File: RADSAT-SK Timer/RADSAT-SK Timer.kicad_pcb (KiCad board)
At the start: 2 copper layers, 90.2 x 95.9 mm, 97 parts, among them J101 Conn_02x26_Odd_Even, J103 Conn_02x26_Odd_Even, J201 Conn_01x04, J203 Conn_01x02, J204 USB_B_Micro, Q101 IRLML2060, Q102 IRLML2060, Q103 IRLML2060, Q104 IRLML2060, Q105 IRLML2060, Q106 IRLML2060, Q107 IRLML2060, Q108 IRLML2060, Q109 IRLML2060, Q201 IRLML2060, SW201 SW_Push, SW202 SW_Push, SW203 SW_Push, SW204 SW_Push, SW205 SW_Push, SW206 SW_Push, U101 LM397MF, U102 LM397MF, U103 LM397MF, U104 CD4052B, U202 LTC3440EMSPBF

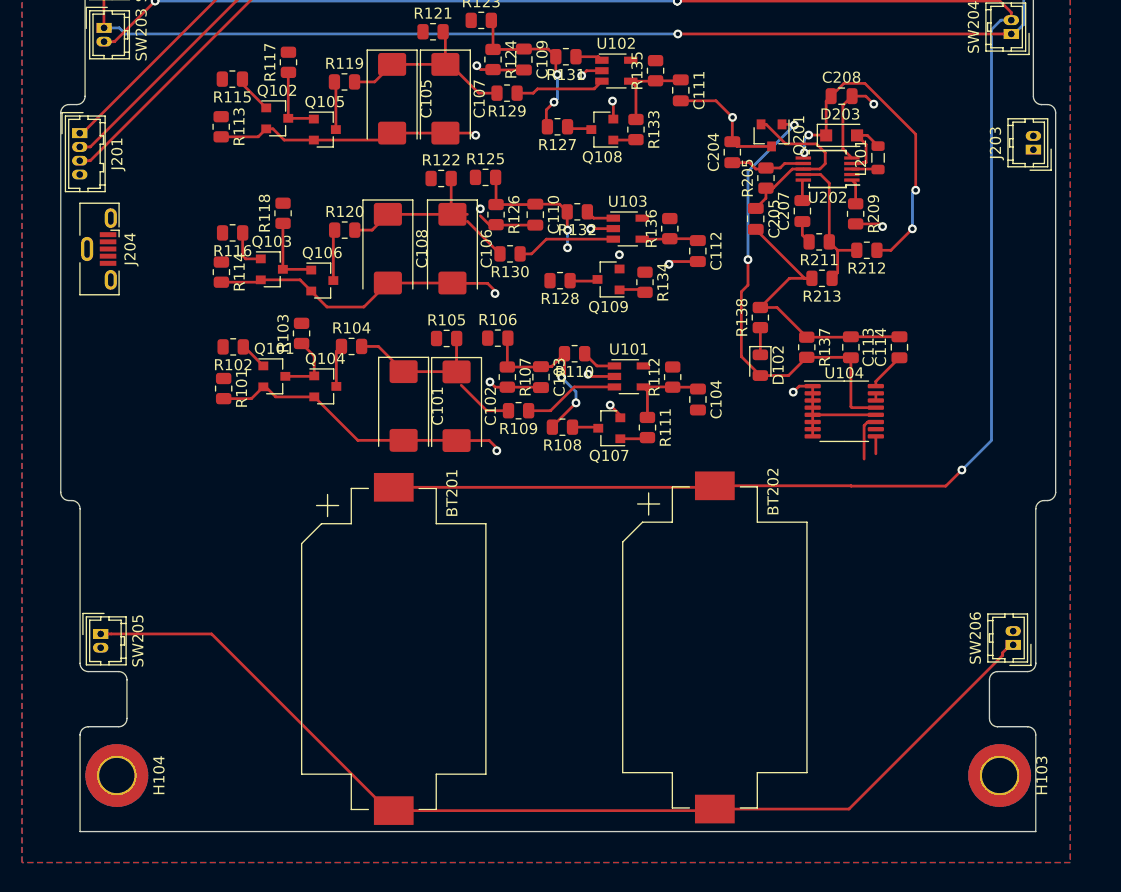
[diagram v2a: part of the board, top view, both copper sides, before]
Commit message: Schematic: Added- 2 more inhibit ports Added- RBF Ports In and Out Connected USb Charger to connector H1-32. Layout: Port positioning and adjustments to some existing circuitry for better tracing.
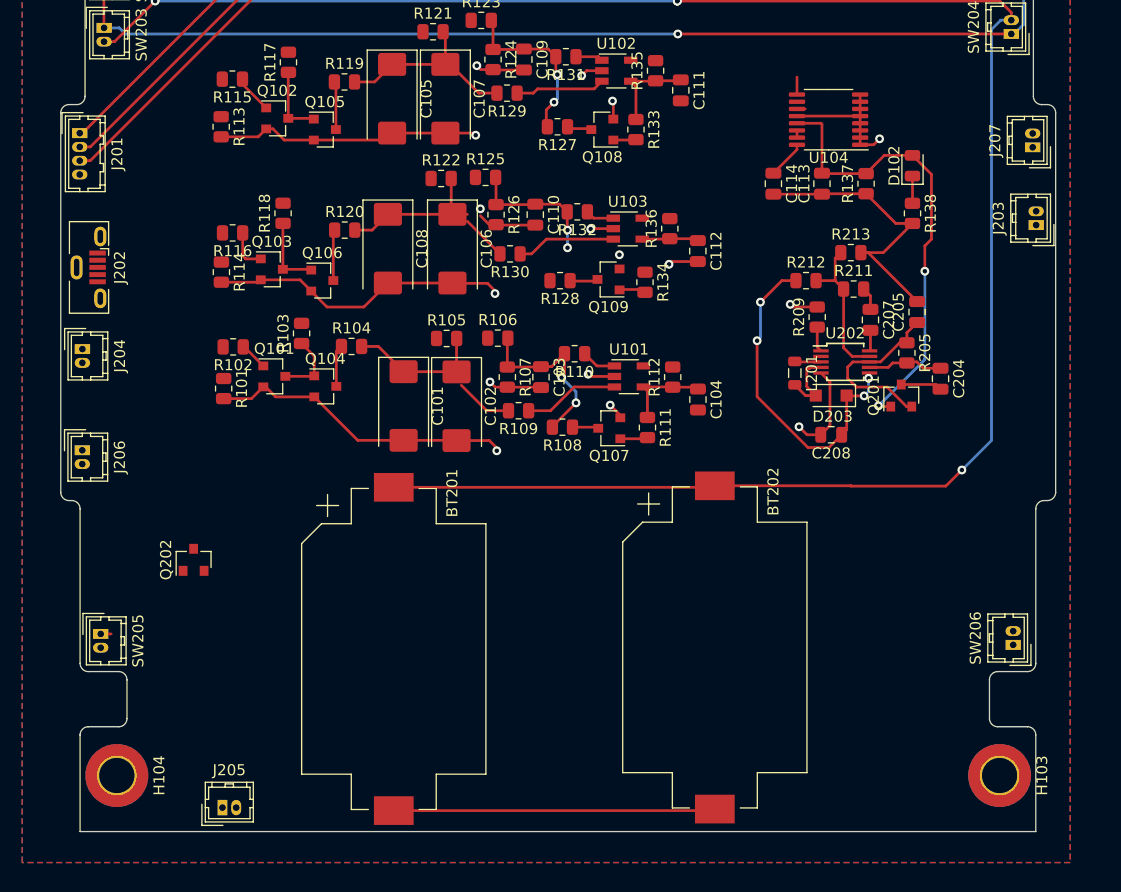
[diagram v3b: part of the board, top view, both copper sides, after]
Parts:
- added J202: USB_B_Micro, Connector_USB:USB_Micro-B_Molex-105133-0001, F.Cu at (37.3, 94.8)
- added J205: Conn_01x02, Connector_Hirose:Hirose_DF13-02P-1.25DSA_1x02_P1.25mm_Vertical, F.Cu at (49.5, 143.7)
- added J206: Conn_01x02, Connector_Hirose:Hirose_DF13-02P-1.25DSA_1x02_P1.25mm_Vertical, F.Cu at (36.8, 111.3)
- added J207: Conn_01x02, Connector_Hirose:Hirose_DF13-02P-1.25DSA_1x02_P1.25mm_Vertical, F.Cu at (122.9, 83.9)
- added Q202: IRLML2060, Package_TO_SOT_SMD:SOT-23, F.Cu at (46.9, 121.3)
- J204: value USB_B_Micro -> Conn_01x02; footprint Connector_USB:USB_Micro-B_Molex-105133-0001 -> Connector_Hirose:Hirose_DF13-02P-1.25DSA_1x02_P1.25mm_Vertical
- moved C208 30.7 mm to (104.7, 109.9), turned to 180 degrees
- moved C204 27.9 mm to (114.6, 104.8), turned to 270 degrees
- moved U104 26.5 mm to (104.4, 81.4), turned to 180 degrees
- moved Q201 26.3 mm to (111.0, 106.4), turned to 90 degrees
- moved D203 23.6 mm to (104.7, 106.4), turned to 180 degrees
- moved D102 22.7 mm to (112.0, 85.5), turned to 90 degrees
- moved L201 20.9 mm to (101.4, 104.3), turned to 270 degrees
- moved R205 20.4 mm to (111.5, 102.5), turned to 270 degrees
- moved C114 18.7 mm to (99.4, 87.2), turned to 270 degrees
- moved U202 17.6 mm to (105.9, 103.3), turned to 0 degrees
- moved C205 16.9 mm to (112.4, 98.8), turned to 90 degrees
- moved R138 16.7 mm to (112.0, 89.9), turned to 270 degrees
- moved R137 15.8 mm to (107.8, 87.2), turned to 90 degrees
- moved C113 15.1 mm to (103.8, 87.2), turned to 270 degrees
- moved C207 11.6 mm to (108.2, 99.5), turned to 270 degrees
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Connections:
- J101 pad 32: (no net) -> USB_Charge
- J204 pad 1: (no net) -> BUS_EN
- J204 pad 2: (no net) -> GND
- SW205 pad 1: Net-(BT201-Pad2) -> Net-(Q202-Pad3)
- SW206 pad 1: Net-(BT201-Pad2) -> Net-(Q202-Pad3)
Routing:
- net Net-(BT201-Pad2): track 95.7 -> 29.7 mm
- net GND: track 172.2 -> 164.7 mm, vias 18 -> 17
- net +BATT: track 38.2 -> 34.7 mm
- net Net-(Q202-Pad3): track 0.00 -> 1.20 mm

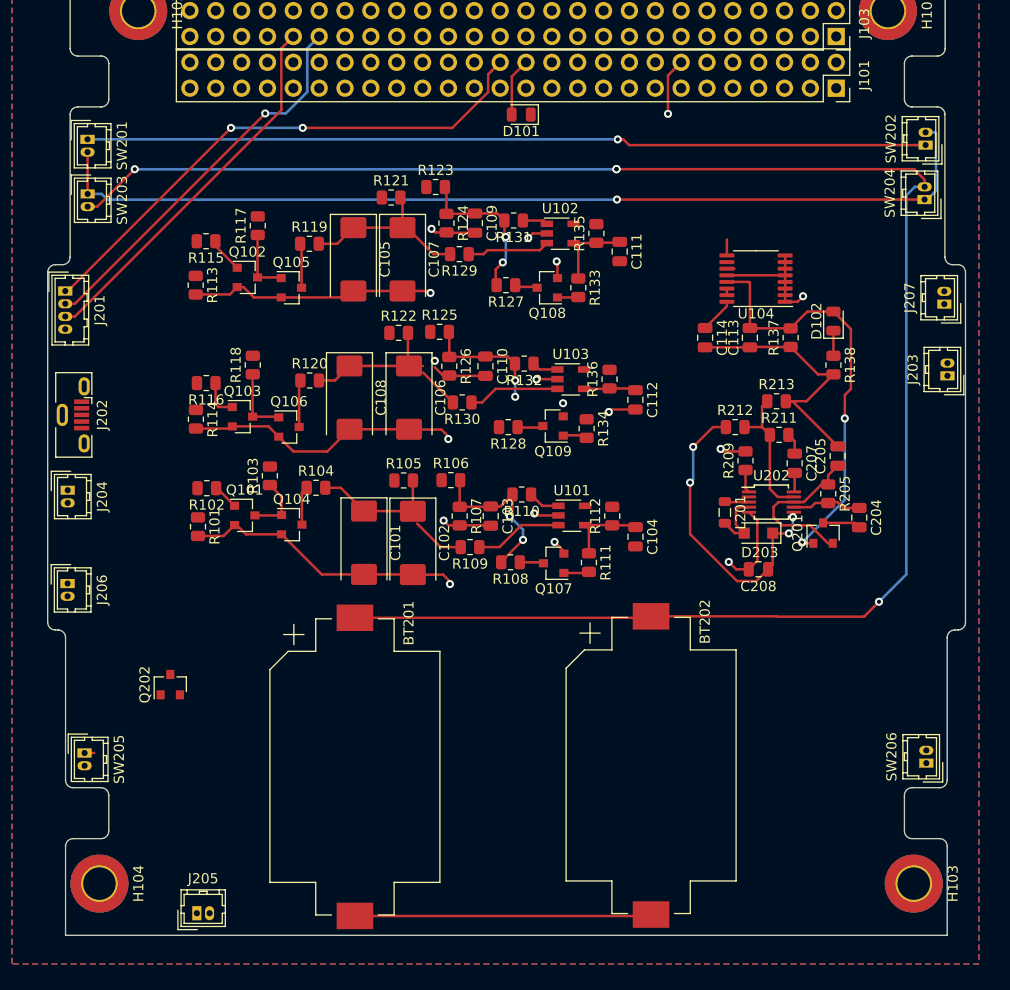
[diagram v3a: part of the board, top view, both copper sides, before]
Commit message: Retraced the board
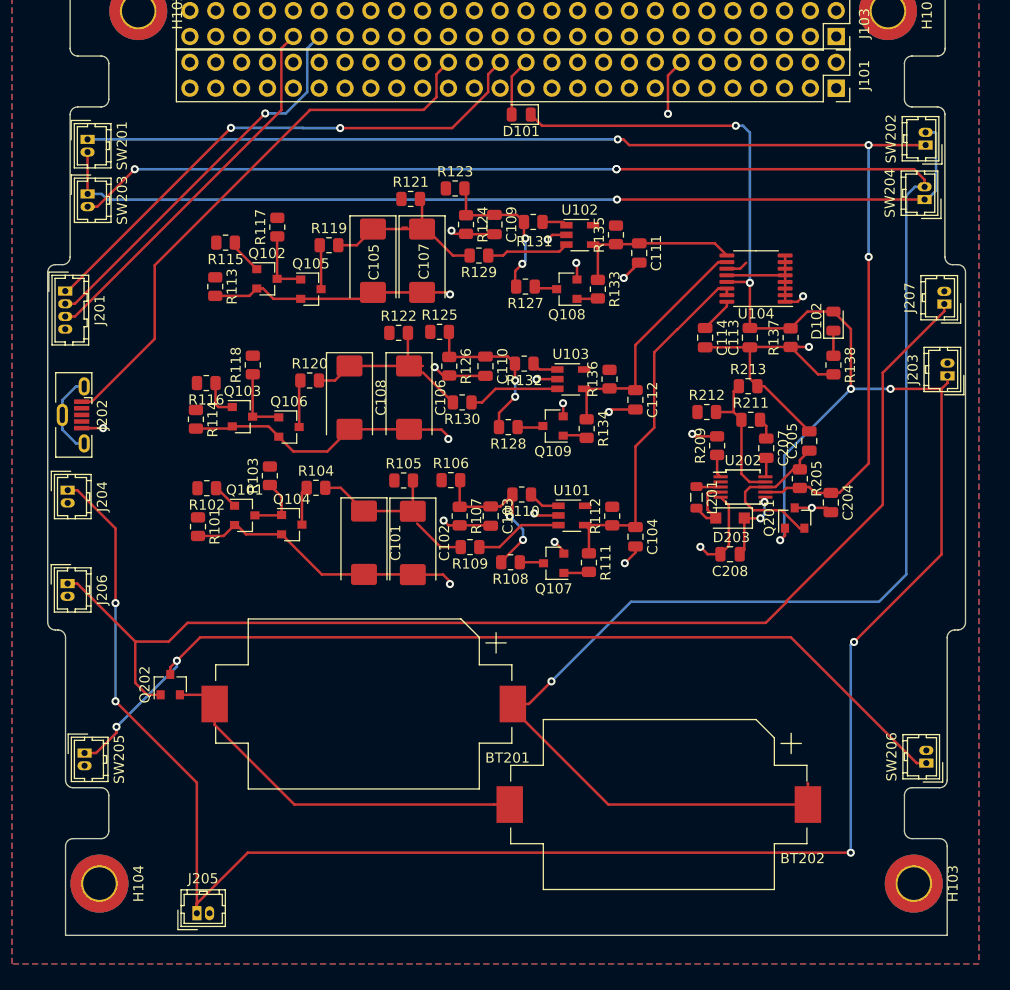
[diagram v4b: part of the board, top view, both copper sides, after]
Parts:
- moved BT201 6.24 mm to (65.9, 123.2), turned to 180 degrees
- moved BT202 3.91 mm to (94.9, 133.0), turned to 180 degrees
- moved C204 3.16 mm to (111.8, 103.4)
- moved C205 3.16 mm to (109.7, 97.3)
- moved Q201 3.16 mm to (108.2, 104.9)
- moved L201 3.16 mm to (98.6, 102.9)
- moved R205 3.16 mm to (108.7, 101.0)
- moved R209 3.16 mm to (100.6, 97.8)
- moved R213 3.16 mm to (103.6, 91.9)
- moved C207 3.16 mm to (105.4, 98.0)
- moved C208 3.16 mm to (101.9, 108.4)
- moved D203 3.16 mm to (101.9, 104.9)
- moved R211 3.16 mm to (103.9, 95.2)
- moved R212 3.16 mm to (99.6, 94.5)
- moved U202 3.16 mm to (103.1, 101.8)
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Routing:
- net BUS_EN: track 42.2 -> 254.5 mm, vias 2 -> 9
- net /RADSAT-SK Timer 2/RBF: track 0.00 -> 117.3 mm
- net Net-(Q202-Pad3): track 1.20 -> 95.2 mm, vias 0 -> 2
- net USB_Charge: track 0.00 -> 55.4 mm
- net Net-(C204-Pad1): track 89.5 -> 125.6 mm, vias 1 -> 3
- net Timer_A_out: track 8.59 -> 36.6 mm
- net Net-(BT201-Pad1): track 180.3 -> 204.1 mm
- net +BATT: track 34.7 -> 14.0 mm, vias 4 -> 2
- net Timer_C_out: track 5.18 -> 25.1 mm
- net Net-(BT201-Pad2): track 29.7 -> 38.1 mm
- net Net-(J202-Pad6): track 0.00 -> 8.32 mm
- net Timer_B_out: track 9.83 -> 17.4 mm
- net GND: track 164.7 -> 171.6 mm, vias 17 -> 22
- net Net-(C110-Pad1): track 12.3 -> 15.9 mm

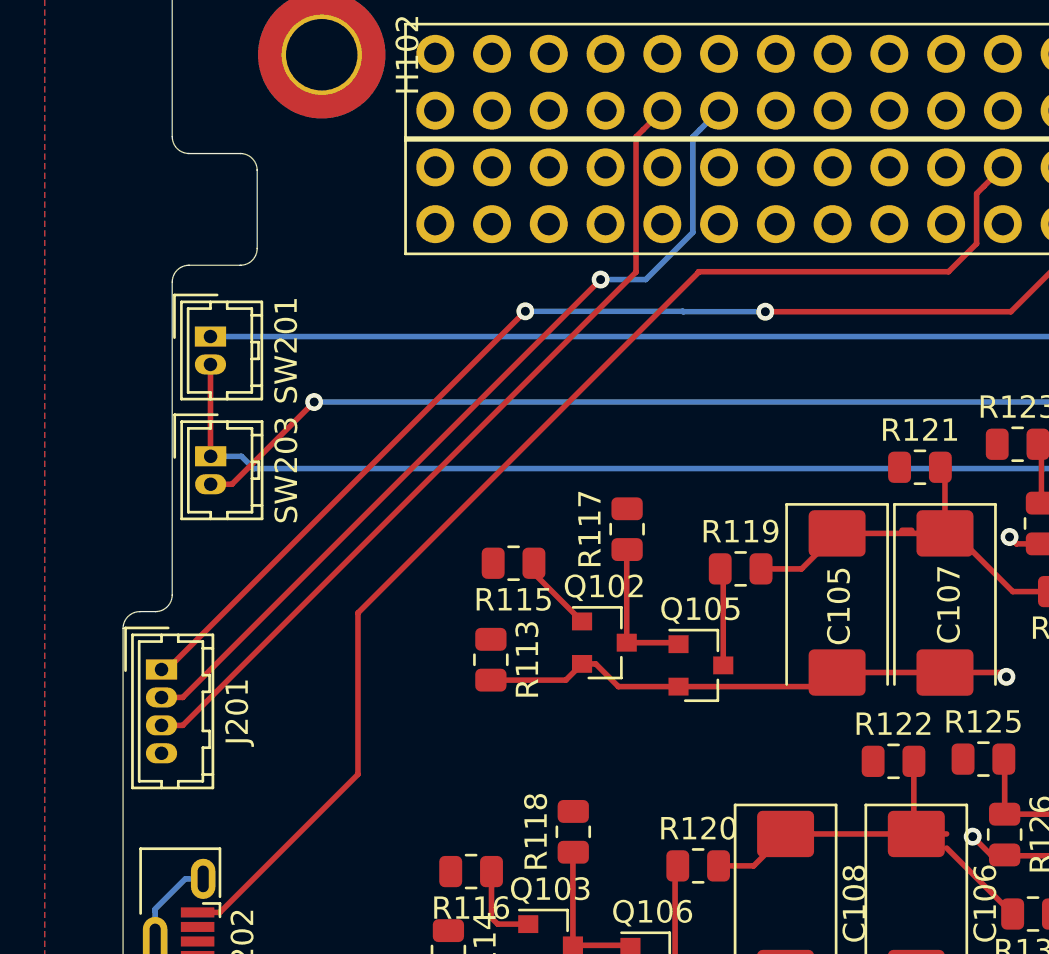
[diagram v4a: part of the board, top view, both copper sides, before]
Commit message: Change to the 7 pin Antenna on the PCB
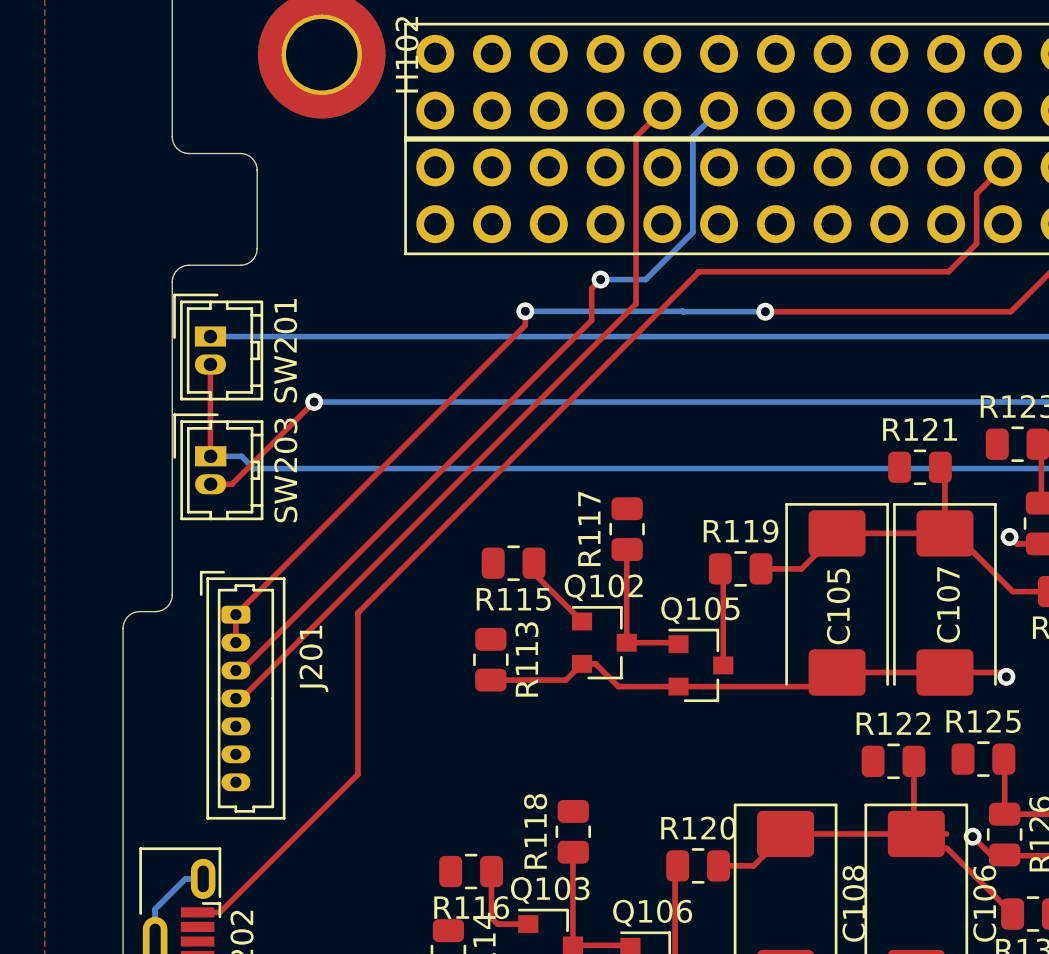
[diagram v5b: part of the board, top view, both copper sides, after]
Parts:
- J201: footprint Connector_Hirose:Hirose_DF13-04P-1.25DSA_1x04_P1.25mm_Vertical -> Connector_Molex:Molex_PicoBlade_53047-0710_1x07_P1.25mm_Vertical
- moved J201 4.13 mm to (39.9, 80.1)
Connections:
- J201 pad 2: I2C_DATA -> +3V3
- J201 pad 3: I2C_CLK -> I2C_DATA
- J201 pad 4: GND -> I2C_CLK
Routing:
- net I2C_CLK: track 37.3 -> 34.4 mm
- net I2C_DATA: track 38.3 -> 35.3 mm
- net +3V3: track 53.1 -> 50.3 mm
